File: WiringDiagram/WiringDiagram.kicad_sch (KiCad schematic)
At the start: 54 parts, among them J1 Conn_01x06, J2 Conn_01x02, J3 Conn_01x04, J4 Conn_01x04, J5 Conn_01x06, J6 Conn_01x08, J8 FTDI SERIAL, SW1 TELEMETRUM ROTARY SWITCH, SW2 ERS SENDER ROTARY SWITCH, SW3 CAMERA BOARD ROTARY SWITCH

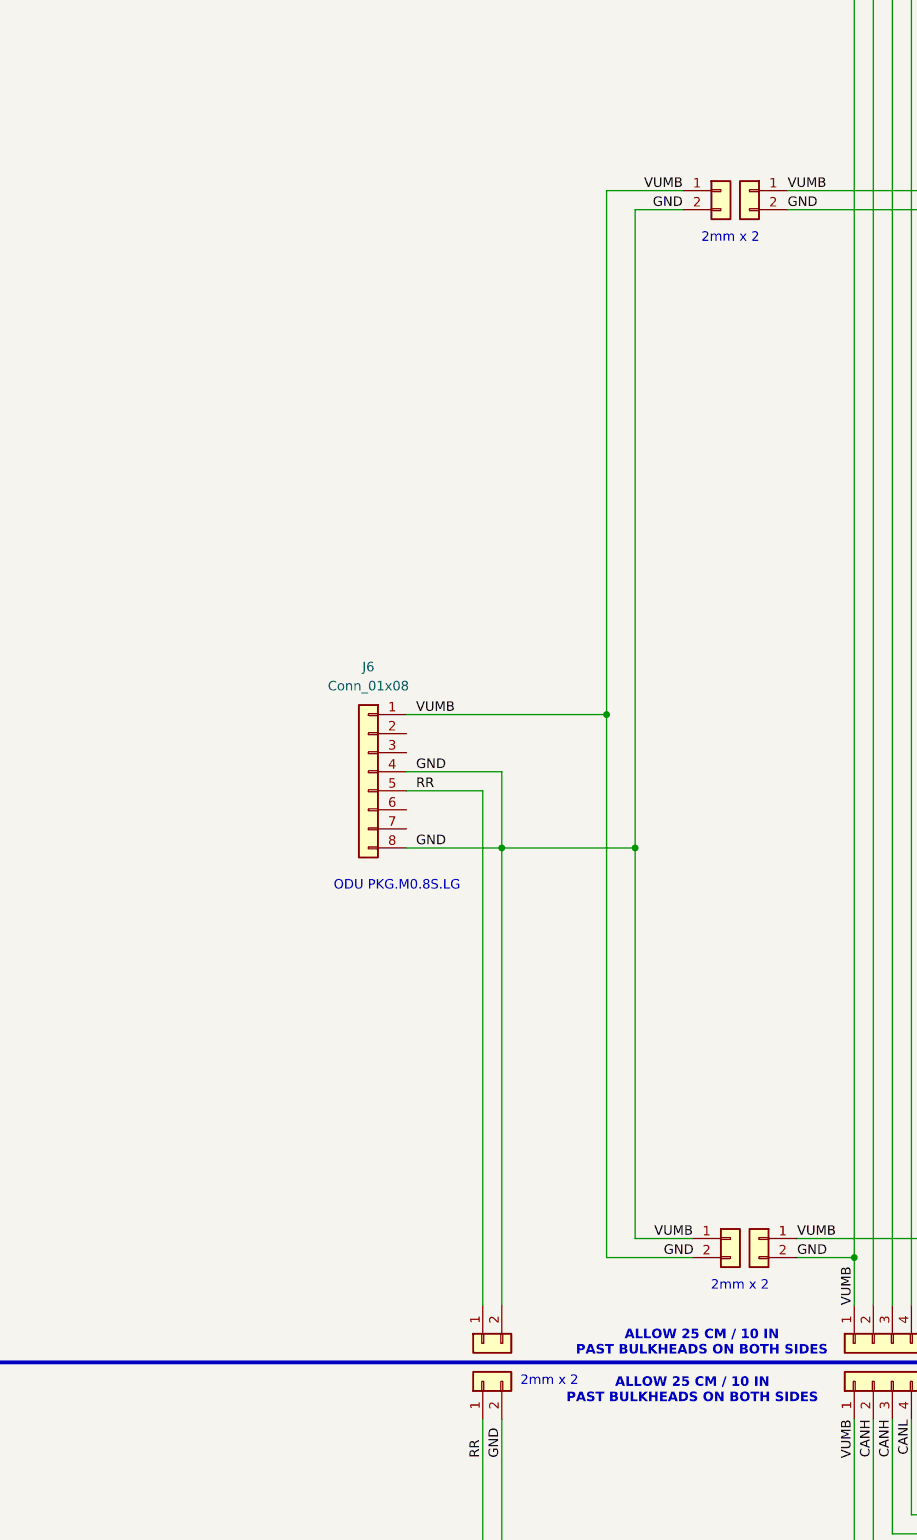
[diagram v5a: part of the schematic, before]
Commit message: Added umbilical cable adapter with labels
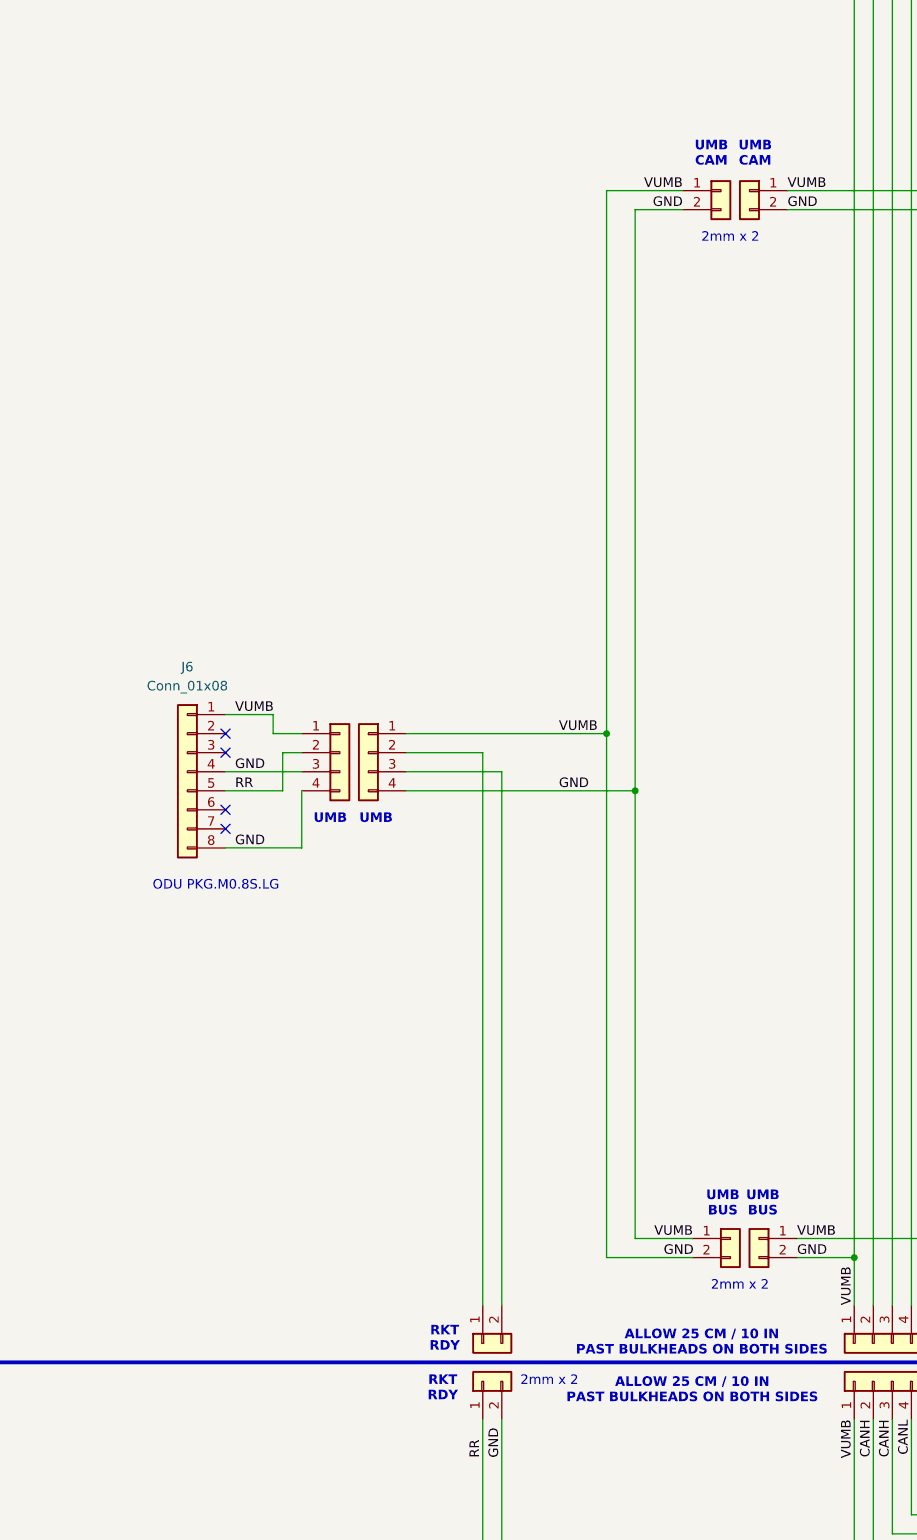
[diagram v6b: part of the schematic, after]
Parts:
- added J7, J9: Conn_01x04, symbol Connector_Generic:Conn_01x04
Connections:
- net GND: now also J7.1 (Pin_1), J7.3 (Pin_3), J7.4 (Pin_4), J9.1 (Pin_1), J9.4 (Pin_4); no longer ERS-J5.2 (Pin_2)
- net RR: now also J7.2 (Pin_2); no longer ERS-J5.1 (Pin_1)
- new net: ERS-J5.1 (Pin_1), J9.2 (Pin_2)
- new net: ERS-J5.2 (Pin_2), J9.3 (Pin_3)
- no-connect marks 3 -> 7
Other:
- note added: "RKT RDY"
- note added: "UMB"
- note added: "UMB BUS"
- note added: "UMB CAM"
- moved on the sheet: J6
